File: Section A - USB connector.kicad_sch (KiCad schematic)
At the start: 5 parts, among them J2 USB4135-GF-A_REVA

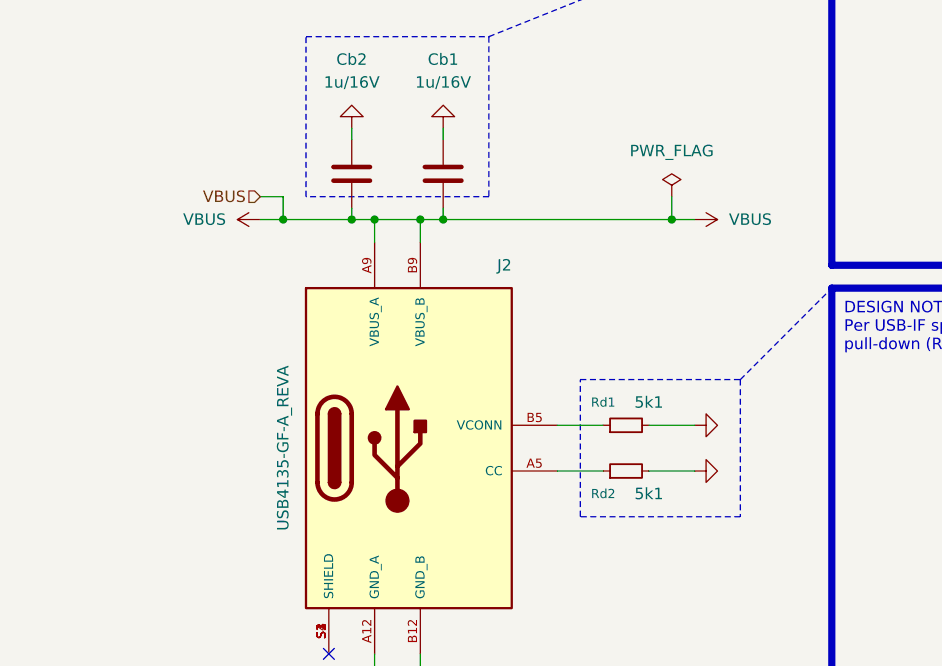
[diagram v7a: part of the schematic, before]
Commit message: screw interface update - changed pinout
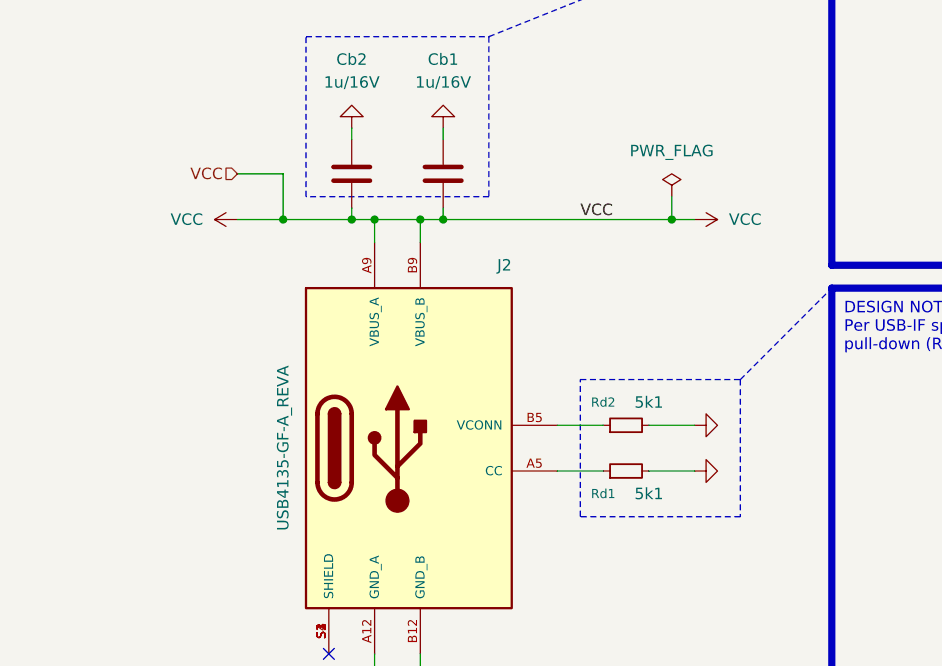
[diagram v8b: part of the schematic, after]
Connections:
- net at Rd2.1: now also J2.B5 (VCONN); no longer J2.A5 (CC)
- net at Rd1.1: now also J2.A5 (CC); no longer J2.B5 (VCONN)
- net VBUS renamed VCC
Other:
- moved on the sheet: Rd1, Rd2
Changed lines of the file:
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@@
 	(wire
 		(pts
-			(xy 86.36 81.28) (xy 88.9 81.28)
+			(xy 83.82 81.28) (xy 88.9 81.28)
 		)
 		(stroke
@@
 	(wire
 		(pts
-			(xy 86.36 78.74) (xy 88.9 78.74)
+			(xy 83.82 76.2) (xy 88.9 76.2)
 		)
 		(stroke
@@
 	(wire
 		(pts
-			(xy 88.9 78.74) (xy 88.9 81.28)
+			(xy 88.9 76.2) (xy 88.9 81.28)
 		)
 		(stroke
@@
 		)
 	)
-	(hierarchical_label "VBUS"
+	(label "VCC"
+		(at 121.92 81.28 0)
+		(effects
+			(font
+				(size 1.27 1.27)
+			)
+			(justify left bottom)
+		)
+	)
+	(hierarchical_label "VCC"
 		(shape input)
-		(at 86.36 78.74 180)
+		(at 83.82 76.2 180)
 		(effects
 			(font
@@
 	(symbol
 		(lib_id "Device:R_Small")
-		(at 127 109.22 90)
+		(at 127 104.14 90)
 		(unit 1)
 		(exclude_from_sim no)
@@
 		(dnp no)
 		(property "Reference" "Rd2"
-			(at 124.46 111.76 90)
+			(at 124.46 101.6 90)
 			(effects
 				(font
@@
 		)
 		(property "Value" "5k1"
-			(at 129.54 111.76 90)
+			(at 129.54 101.6 90)
 			(effects
 				(font
@@
 		)
 		(property "Footprint" "Resistor_SMD:R_0805_2012Metric"
-			(at 127 109.22 0)
+			(at 127 104.14 0)
 			(effects
 				(font
@@
 		)
 		(property "Datasheet" "~"
-			(at 127 109.22 0)
+			(at 127 104.14 0)
 			(effects
 				(font
@@
 		)
 		(property "Description" "Resistor, small symbol"
-			(at 127 109.22 0)
+			(at 127 104.14 0)
 			(effects
 				(font
@@
 	)
 	(symbol
-		(lib_id "power:VBUS")
-		(at 134.62 81.28 270)
-		(unit 1)
-		(exclude_from_sim no)
-		(in_bom yes)
-		(on_board yes)
-		(dnp no)
-		(fields_autoplaced yes)
-		(property "Reference" "#PWR02"
-			(at 130.81 81.28 0)
-			(effects
-				(font
-					(size 1.27 1.27)
-				)
-				(hide yes)
-			)
-		)
-		(property "Value" "VBUS"
-			(at 138.43 81.2799 90)
-			(effects
-				(font
-					(size 1.27 1.27)
-				)
-				(justify left)
-			)
-		)
-		(property "Footprint" ""
-			(at 134.62 81.28 0)
-			(effects
-				(font
-					(size 1.27 1.27)
-				)
-				(hide yes)
-			)
-		)
-		(property "Datasheet" ""
-			(at 134.62 81.28 0)
-			(effects
-				(font
-					(size 1.27 1.27)
-				)
-				(hide yes)
-			)
-		)
-		(property "Description" "Power symbol creates a global label with name \"VBUS\""
-			(at 134.62 81.28 0)
-			(effects
-				(font
-					(size 1.27 1.27)
-				)
-				(hide yes)
-			)
-		)
-		(pin "1"
-		)
-		(instances
-			(project ""
-				(path "/f9e05184-c88b-4a88-ae9c-ab2bdb32be7c/c5103ceb-5325-4a84-a025-9638a412984e/f06537ee-772d-44d3-8c50-e0ba41038c9c"
-					(reference "#PWR02")
-					(unit 1)
-				)
-			)
-		)
-	)
-	(symbol
 		(lib_id "power:GND")
 		(at 134.62 104.14 90)
@@
 	)
 	(symbol
-		(lib_id "power:VBUS")
-		(at 86.36 81.28 90)
+		(lib_id "power:GND")
+		(at 83.82 134.62 270)
 		(unit 1)
 		(exclude_from_sim no)
@@
 		(dnp no)
 		(fields_autoplaced yes)
-		(property "Reference" "#PWR017"
-			(at 90.17 81.28 0)
+		(property "Reference" "#PWR01"
+			(at 77.47 134.62 0)
 			(effects
 				(font
@@
 			)
 		)
-		(property "Value" "VBUS"
-			(at 82.55 81.2799 90)
+		(property "Value" "GND"
+			(at 78.74 134.62 0)
 			(effects
 				(font
 					(size 1.27 1.27)
 				)
-				(justify left)
+				(hide yes)
 			)
 		)
 		(property "Footprint" ""
-			(at 86.36 81.28 0)
+			(at 83.82 134.62 0)
 			(effects
 				(font
@@
 		)
 		(property "Datasheet" ""
-			(at 86.36 81.28 0)
+			(at 83.82 134.62 0)
 			(effects
 				(font
@@
 			)
 		)
-		(property "Description" "Power symbol creates a global label with name \"VBUS\""
-			(at 86.36 81.28 0)
+		(property "Description" "Power symbol creates a global label with name \"GND\" , ground"
+			(at 83.82 134.62 0)
 			(effects
 				(font
@@
 			(project "Sienkiewicz_TOUCH"
 				(path "/f9e05184-c88b-4a88-ae9c-ab2bdb32be7c/c5103ceb-5325-4a84-a025-9638a412984e/f06537ee-772d-44d3-8c50-e0ba41038c9c"
-					(reference "#PWR017")
+					(reference "#PWR01")
 					(unit 1)
 				)
@@
 	)
 	(symbol
-		(lib_id "power:GND")
-		(at 83.82 134.62 270)
+		(lib_id "power:VCC")
+		(at 83.82 81.28 90)
 		(unit 1)
 		(exclude_from_sim no)
@@
 		(dnp no)
 		(fields_autoplaced yes)
-		(property "Reference" "#PWR01"
-			(at 77.47 134.62 0)
+		(property "Reference" "#PWR02"
+			(at 87.63 81.28 0)
 			(effects
 				(font
@@
 			)
 		)
-		(property "Value" "GND"
-			(at 78.74 134.62 0)
+		(property "Value" "VCC"
+			(at 80.01 81.2799 90)
+			(effects
+				(font
+					(size 1.27 1.27)
+				)
+				(justify left)
+			)
+		)
+		(property "Footprint" ""
+			(at 83.82 81.28 0)
+			(effects
+				(font
+					(size 1.27 1.27)
+				)
+				(hide yes)
+			)
+		)
+		(property "Datasheet" ""
+			(at 83.82 81.28 0)
+			(effects
+				(font
+					(size 1.27 1.27)
+				)
+				(hide yes)
+			)
+		)
+		(property "Description" "Power symbol creates a global label with name \"VCC\""
+			(at 83.82 81.28 0)
 			(effects
 				(font
@@
 			)
 		)
+		(pin "1"
+		)
+		(instances
+			(project ""
+				(path "/f9e05184-c88b-4a88-ae9c-ab2bdb32be7c/c5103ceb-5325-4a84-a025-9638a412984e/f06537ee-772d-44d3-8c50-e0ba41038c9c"
+					(reference "#PWR02")
+					(unit 1)
+				)
+			)
+		)
+	)
+	(symbol
+		(lib_id "power:VCC")
+		(at 134.62 81.28 270)
+		(unit 1)
+		(exclude_from_sim no)
+		(in_bom yes)
+		(on_board yes)
+		(dnp no)
+		(fields_autoplaced yes)
+		(property "Reference" "#PWR017"
+			(at 130.81 81.28 0)
+			(effects
+				(font
+					(size 1.27 1.27)
+				)
+				(hide yes)
+			)
+		)
+		(property "Value" "VCC"
+			(at 138.43 81.2799 90)
+			(effects
+				(font
+					(size 1.27 1.27)
+				)
+				(justify left)
+			)
+		)
 		(property "Footprint" ""
-			(at 83.82 134.62 0)
+			(at 134.62 81.28 0)
 			(effects
 				(font
@@
 		)
 		(property "Datasheet" ""
-			(at 83.82 134.62 0)
+			(at 134.62 81.28 0)
 			(effects
 				(font
@@
 			)
 		)
-		(property "Description" "Power symbol creates a global label with name \"GND\" , ground"
-			(at 83.82 134.62 0)
+		(property "Description" "Power symbol creates a global label with name \"VCC\""
+			(at 134.62 81.28 0)
 			(effects
 				(font
@@
 			(project "Sienkiewicz_TOUCH"
 				(path "/f9e05184-c88b-4a88-ae9c-ab2bdb32be7c/c5103ceb-5325-4a84-a025-9638a412984e/f06537ee-772d-44d3-8c50-e0ba41038c9c"
-					(reference "#PWR01")
+					(reference "#PWR017")
 					(unit 1)
 				)
@@
 	(symbol
 		(lib_id "Device:R_Small")
-		(at 127 104.14 90)
+		(at 127 109.22 90)
 		(unit 1)
 		(exclude_from_sim no)
@@
 		(dnp no)
 		(property "Reference" "Rd1"
-			(at 124.46 101.6 90)
+			(at 124.46 111.76 90)
 			(effects
 				(font
@@
 		)
 		(property "Value" "5k1"
-			(at 129.54 101.6 90)
+			(at 129.54 111.76 90)
 			(effects
 				(font
@@
 		)
 		(property "Footprint" "Resistor_SMD:R_0805_2012Metric"
-			(at 127 104.14 0)
+			(at 127 109.22 0)
 			(effects
 				(font
@@
 		)
 		(property "Datasheet" "~"
-			(at 127 104.14 0)
+			(at 127 109.22 0)
 			(effects
 				(font
@@
 		)
 		(property "Description" "Resistor, small symbol"
-			(at 127 104.14 0)
+			(at 127 109.22 0)
 			(effects
 				(font
